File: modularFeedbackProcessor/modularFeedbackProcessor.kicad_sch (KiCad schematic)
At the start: 31 parts, among them J1 AudioJack2_SwitchT, Q1 NJFET, U1 V3205, U2 CD4046, U3 LM358, U4 RC4558, U5 LM13700, U6 TL074

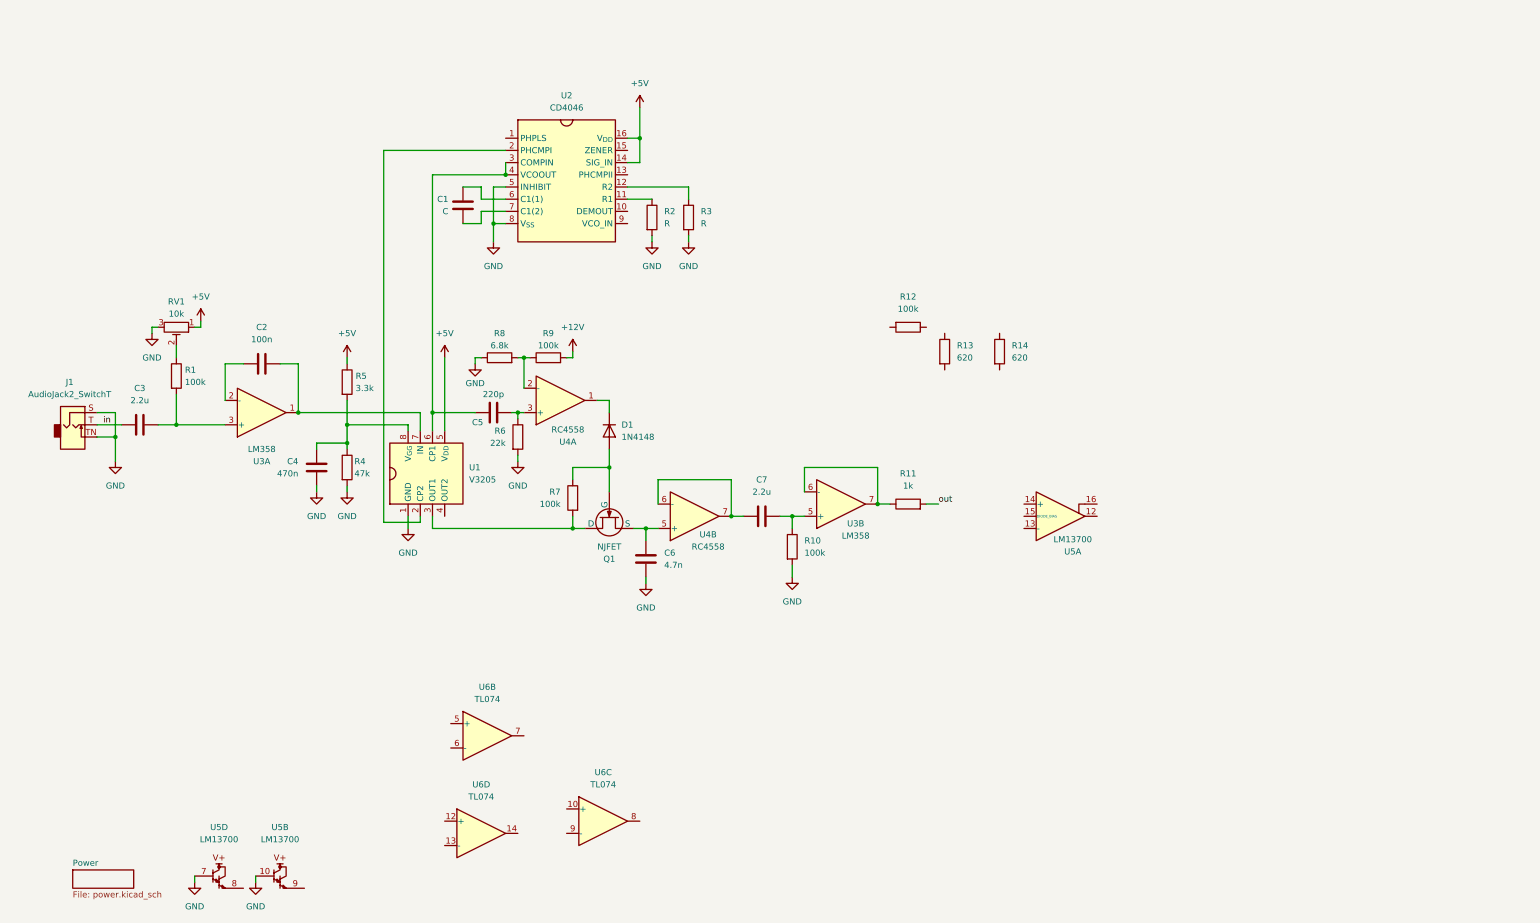
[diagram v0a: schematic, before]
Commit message: Added linked mixer submodule.
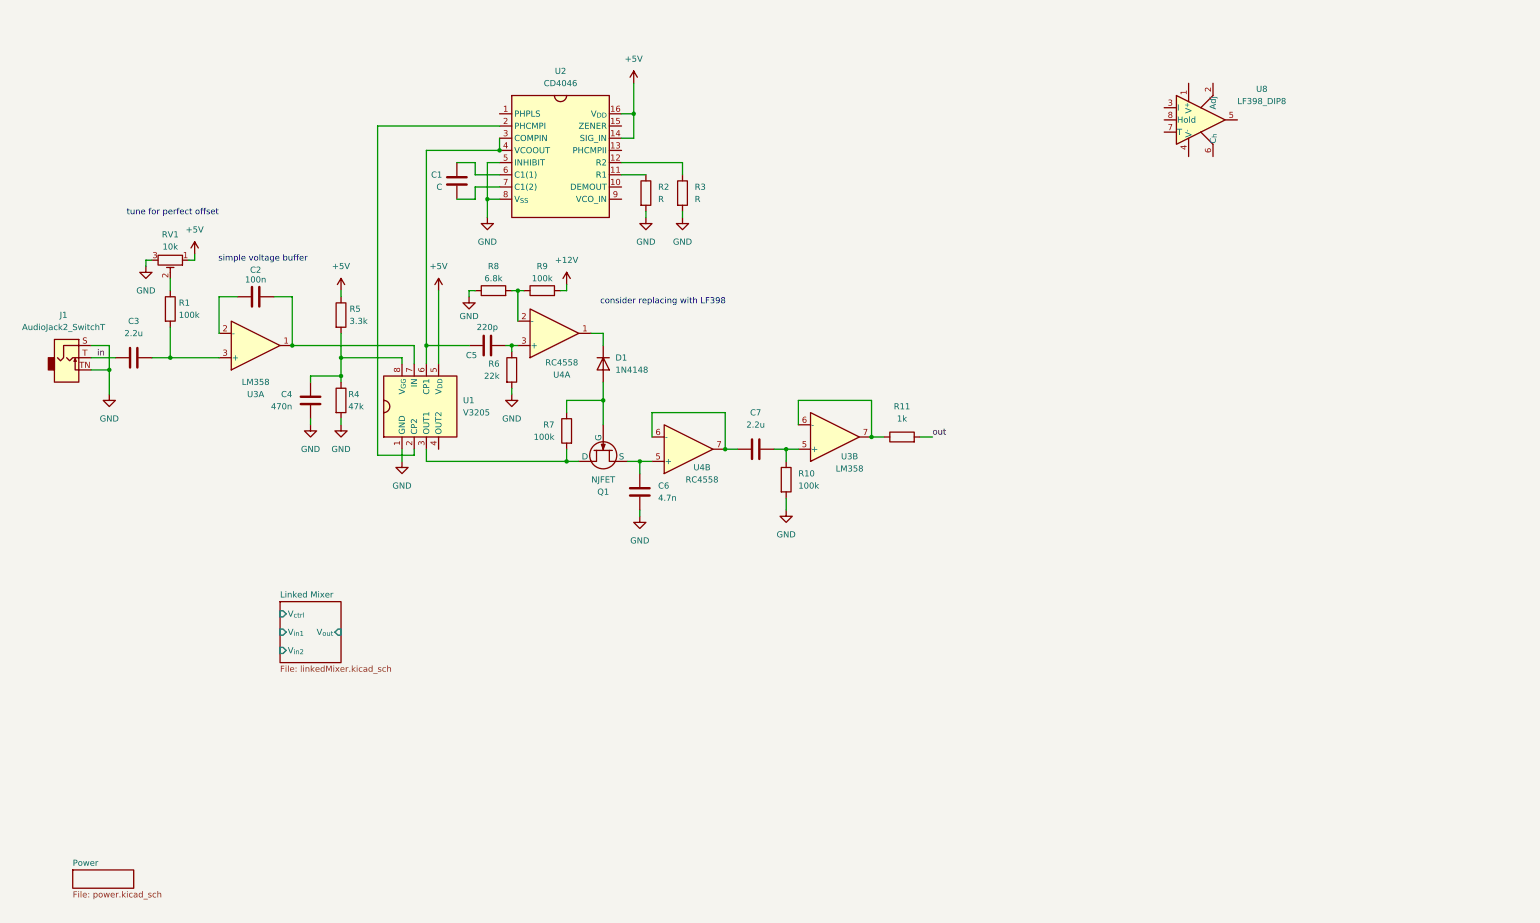
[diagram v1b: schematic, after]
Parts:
- removed R12: 100k, symbol Device:R
- removed R13, R14: 620, symbol Device:R
- removed U5: LM13700, symbol Amplifier_Operational:LM13700
- removed U6: TL074, symbol Amplifier_Operational:TL074
- added unit 2 of U3
- added U8: LF398_DIP8, Package_DIP:DIP-8_W7.62mm, symbol Analog:LF398_DIP8
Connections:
- net at C7.1, R10.1: now also U3.5 (+); no longer U3.5 (+)
- new net: R11.1, U3.6 (-), U3.7
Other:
- added sheet Linked Mixer (linkedMixer.kicad_sch)
- note added: "consider replacing with LF398"
- note added: "simple voltage buffer"
- note added: "tune for perfect offset"
- moved on the sheet: C1, C2, C3, C4, C5, C6, C7, D1, J1, Q1, R1, R10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

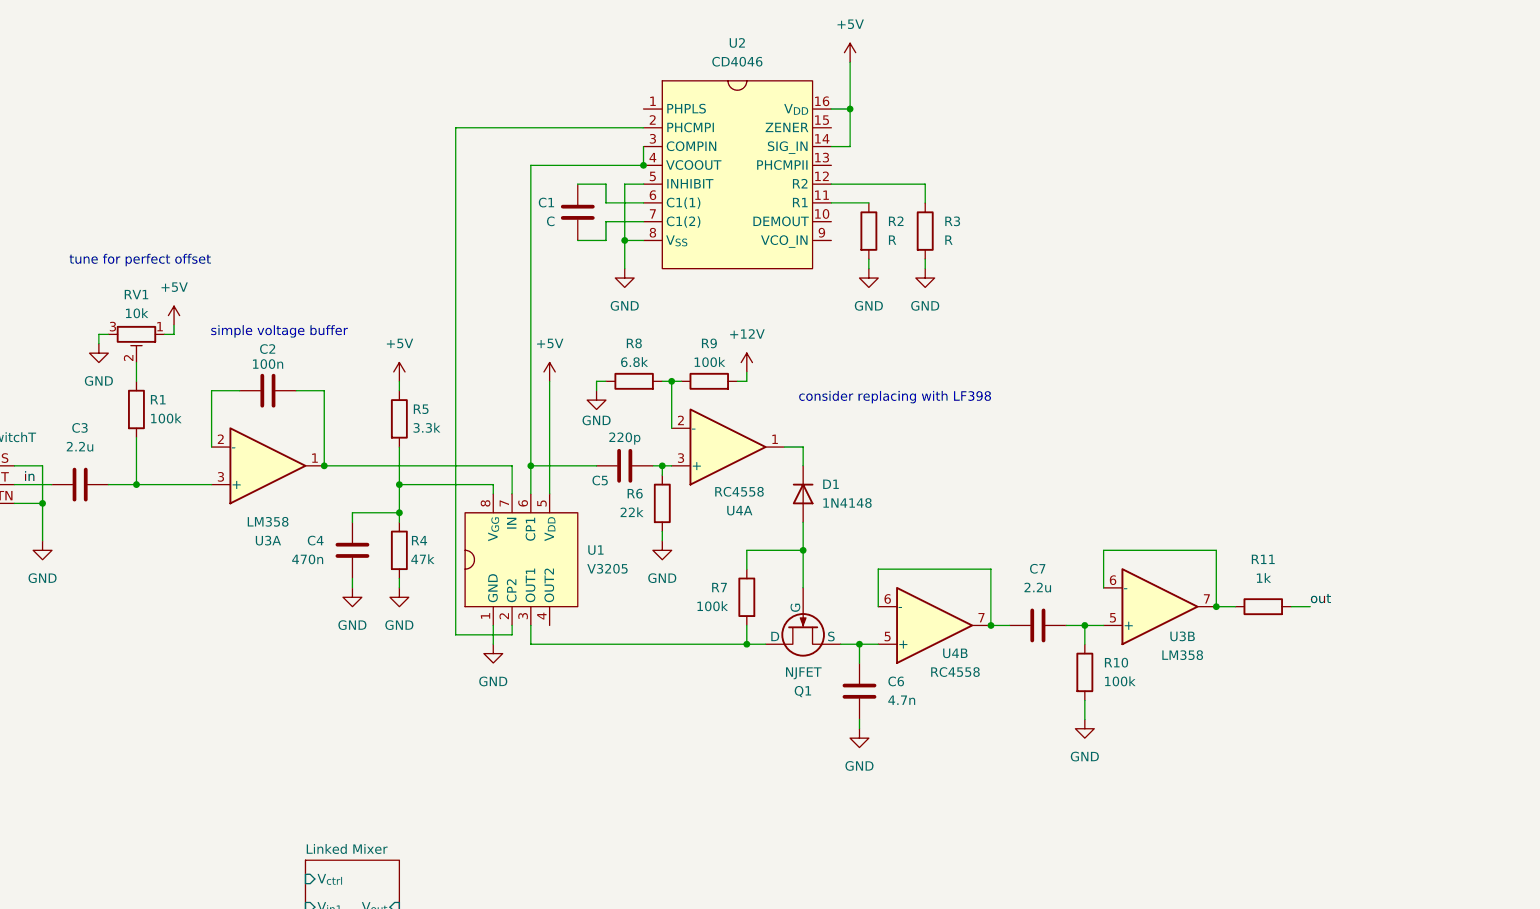
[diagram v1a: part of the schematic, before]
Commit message: Scaling down input from 10Vpp to 1Vpp
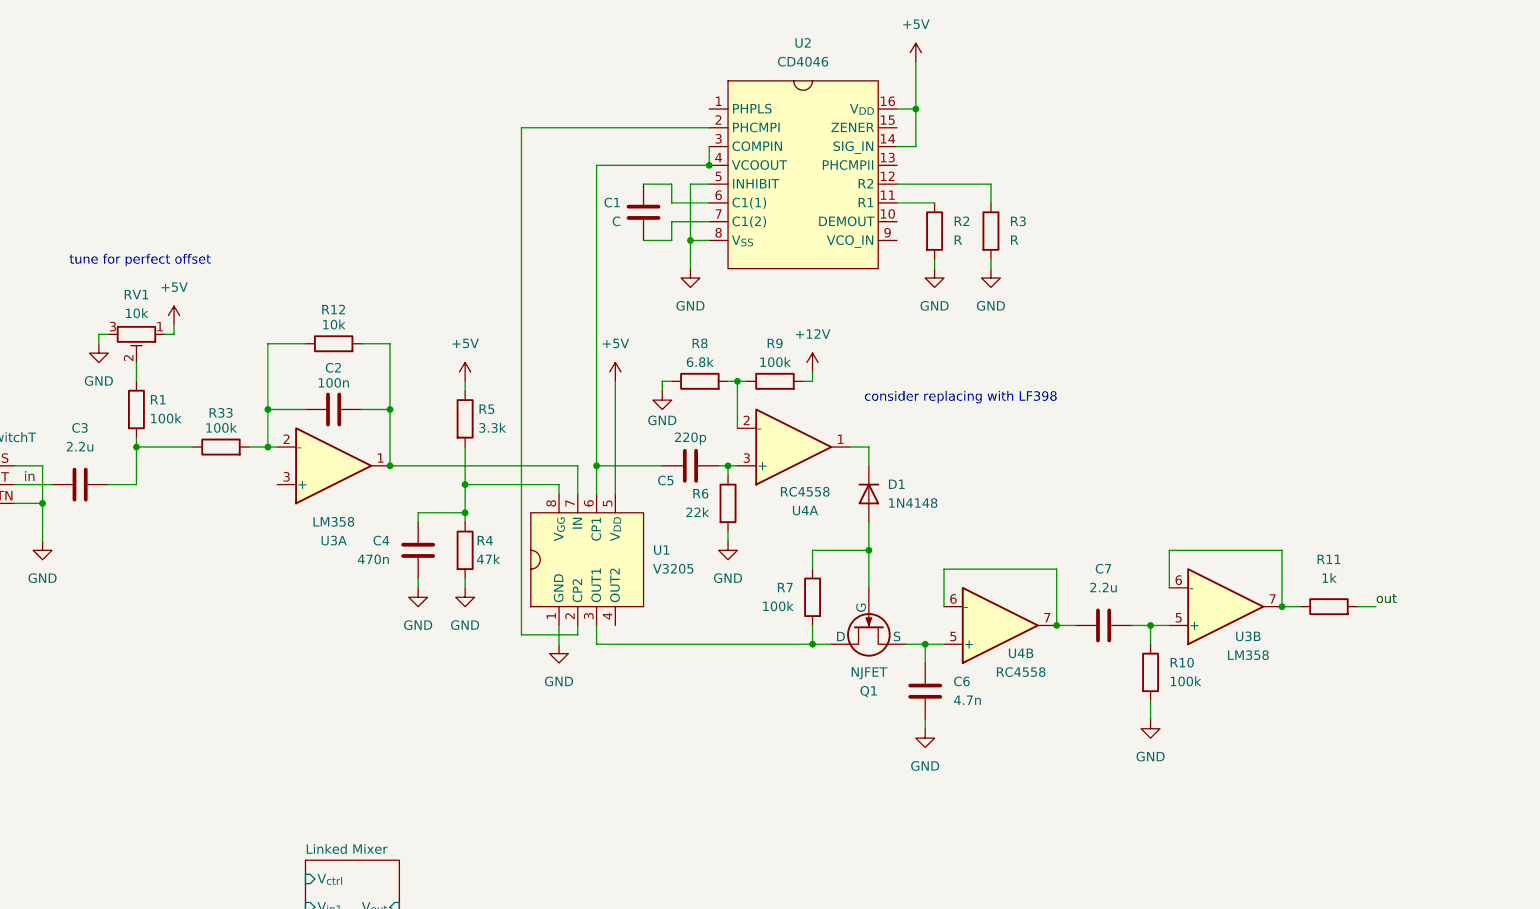
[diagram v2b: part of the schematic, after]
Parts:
- added R12: 10k, symbol Device:R
- added R33: 100k, symbol Device:R
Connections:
- net at C2.2, U1.7 (IN), U3.1: now also R12.2
- net at C2.1, U3.2 (-): now also R12.1, R33.2
- net at C3.2, R1.2: now also R33.1; no longer U3.3 (+)
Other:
- note removed: "simple voltage buffer"
- moved on the sheet: C1, C2, C4, C5, C6, C7, D1, Q1, R10, R11, R2, R3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

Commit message: added basic CV control for single linked mixer
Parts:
- added J2: AudioJack2_SwitchT, symbol Connector_Audio:AudioJack2_SwitchT
- added R34, R35: 330k, symbol Device:R
- added RV5: 10k, symbol Device:R_Potentiometer_Trim
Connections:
- net +5V: now also RV5.1
- net GND: now also J2.S, J2.TN, RV5.3
- net Linked Mixer/V_{ctrl}: now also R34.2, R35.2
- new net: R34.1, RV5.2
- new net: J2.T, R35.1

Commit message: Minor changes + clock CV rework based on Moritz Klein's work
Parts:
- added ClockCV, ClockCVLvl: 100k, symbol Device:R_Potentiometer_Trim
- added D3, D4: 1N4148, Diode_THT:D_DO-35_SOD27_P7.62mm_Horizontal, symbol Diode:1N4148
- added J10: Double, symbol Connector_Audio:AudioJack2_SwitchT
- added J3: Output, symbol Connector_Audio:AudioJack2_SwitchT
- added J4: EffectRouteOut, symbol Connector_Audio:AudioJack2_SwitchT
- added J5: EffectRouteIn, symbol Connector_Audio:AudioJack2_SwitchT
- added J6: Rate, symbol Connector_Audio:AudioJack2_SwitchT
- added J7: Feedback, symbol Connector_Audio:AudioJack2_SwitchT
- added J8: EffectDryWet, symbol Connector_Audio:AudioJack2_SwitchT
- added J9: Inhibit, symbol Connector_Audio:AudioJack2_SwitchT
- added R36, R37: 100k, symbol Device:R
- added R38, R39: 22k, symbol Device:R
- added U6, U9: TL074, symbol Amplifier_Operational:TL074
- C1: value C -> 1n
- J1: value AudioJack2_SwitchT -> Input
- J2: value AudioJack2_SwitchT -> DryWet
- R2: value R -> 39k
- R3: value R -> 2.2Meg
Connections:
- net +5V: now also D4.1 (K), R38.1
- net GND: now also U3.3 (+), ClockCVLvl.3, D3.2 (A), J6.S, J6.TN, R39.1
- net at U2.9 (VCO_IN): now also D3.1 (K), D4.2 (A), R36.1, R37.1
- new net: ClockCVLvl.1, J6.T
- new net: ClockCV.1, R38.2
- new net: ClockCV.2, R37.2
- new net: ClockCV.3, R39.2
- new net: ClockCVLvl.2, R36.2
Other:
- note added: "<- DC block to ground"
- note added: "<- tune for high frequency audio to drive sample and hold"
- note added: "consider replacing SaH with LF398"
- note added: "provide 14/15 V_{DD}"
- note added: "scale from 10Vpp to 1Vpp filter noise"
- note removed: "consider replacing with LF398"
- moved on the sheet: J2, R2, R3, R34, R35, RV5

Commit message: some CV work
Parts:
- added D5, D6: 1N4148, Diode_THT:D_DO-35_SOD27_P7.62mm_Horizontal, symbol Diode:1N4148
- added R40: 100k, symbol Device:R
- R3: value 2.2Meg -> 330k
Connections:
- net +5V: now also D5.1 (K)
- net GND: now also J9.S, J9.TN, D6.2 (A); no longer U2.5 (INHIBIT)
- net at J9.T: now also R40.1
- new net: D5.2 (A), D6.1 (K), R40.2, U2.5 (INHIBIT)
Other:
- note added: "clock CV circuit (credit to MK)"
- note added: "inhibit circuit (default ground)"
- moved on the sheet: C1, J9

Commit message: last lab changes. slightly more text
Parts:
- added DryWetCVLvl: 10k, symbol Device:R_Potentiometer_Trim
- renumbered RV5 to DryWetCV
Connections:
- net GND: now also DryWetCVLvl.3
- net at R35.1: now also DryWetCVLvl.2; no longer J2.T
- new net: DryWetCVLvl.1, J2.T
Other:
- note added: "REMEMBER TO SCALE AUDIO BACK UP"
- note added: "buffer after block+bias"
- note added: "clipping diodes in feedback path to eliminate extremely large voltages"
- note added: "scale from 10Vpp to 1Vpp + filter noise"
- note removed: "scale from 10Vpp to 1Vpp filter noise"
- moved on the sheet: DryWetCV, J2, J3, J4, J5, J6, J7, J8, R34, R35, U8
